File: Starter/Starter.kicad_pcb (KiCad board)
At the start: 2 copper layers, 114.3 x 88.9 mm, 51 parts, among them J1 AudioJack, J2 Speaker, J3 UART1, J4 Pot, J5 Conn_01x08_Pin, J6 GND, J7 DACOUT, SW1 UP, SW2 LEFT, SW3 DOWN, SW4 RGHT, U1 Adafruit ST7735R, U2 LP-MSPM0G3507, U3 MCP34119P, U4 HiLetGo_ST7735R, U5 ULN2003B, U6 TSOP31438

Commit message: update from sch
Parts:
- removed C1: 1uF, ECE319K:CP_Radial_Tantal200mil
- removed C2: 4.7uF, ECE319K:CP_Radial_Tantal200mil
- removed G***: LOGO, LOGO
- removed J1: AudioJack, ECE319K:Jack_3.5mm_CUI_SJ1-3523N_Horizontal
- removed J3: UART1, ECE319K:PinHeader_1x03_P2.54mm_Vertical
- removed J4: Pot, ECE319K:Testpoint_1x02_P2.54mm
- removed J6: GND, ECE319K:Testpoint_1x02_P2.54mm
- removed J7: DACOUT, ECE319K:Testpoint_1x02_P2.54mm
- removed JP1: TExaS, ECE319K:PinHeader_1x03_P2.54mm_Vertical
- removed R10: 12k, ECE319K:R_Axial_DIN0204_L3.6mm_D1.6mm_P7.62mm_Horizontal
- removed R17: 10k, ECE319K:R_Axial_DIN0204_L3.6mm_D1.6mm_P7.62mm_Horizontal
- removed U1: Adafruit ST7735R, ECE319K:adafruit_st7735r
- added C13: 0.1uF, Capacitor_SMD:C_0603_1608Metric_Pad1.08x0.95mm_HandSolder, F.Cu at (161.2, 124.7)
- added C14: 1uF, Capacitor_SMD:C_0603_1608Metric_Pad1.08x0.95mm_HandSolder, F.Cu at (161.2, 127.2)
- added C15: 4.7uF, Capacitor_SMD:C_0603_1608Metric_Pad1.08x0.95mm_HandSolder, F.Cu at (161.2, 129.7)
- added C16: 10nF, Capacitor_SMD:C_0603_1608Metric_Pad1.08x0.95mm_HandSolder, F.Cu at (165.5, 109.6)
- added C17: 0.1uF, Capacitor_SMD:C_0603_1608Metric_Pad1.08x0.95mm_HandSolder, F.Cu at (165.5, 112.1)
- added C18: 2.2uF, Capacitor_SMD:C_0603_1608Metric_Pad1.08x0.95mm_HandSolder, F.Cu at (165.5, 114.6)
- added C5: 0.1uF, Capacitor_SMD:C_0603_1608Metric_Pad1.08x0.95mm_HandSolder, F.Cu at (161.2, 114.6)
- added C6: 0.1uF, Capacitor_SMD:C_0603_1608Metric_Pad1.08x0.95mm_HandSolder, F.Cu at (161.2, 117.1)
- added C7: 0.1uF, Capacitor_SMD:C_0603_1608Metric_Pad1.08x0.95mm_HandSolder, F.Cu at (161.2, 119.7)
- added C8: 0.1uF, Capacitor_SMD:C_0603_1608Metric_Pad1.08x0.95mm_HandSolder, F.Cu at (161.2, 122.2)
- added D5: LED, LED_SMD:LED_0805_2012Metric, F.Cu at (189.4, 122.0)
- added D6: LED, LED_SMD:LED_0805_2012Metric, F.Cu at (189.4, 125.1)
- added D7: S1A, Diode_SMD:D_SMA, F.Cu at (189.2, 105.7)
- added M1: Vibration Motor, ECE319K:Testpoint_1x02_P2.54mm, F.Cu at (192.1, 98.6)
- added MT1: ICM-42670-P, ECE319K:XDCR_ICM-42670-P, F.Cu at (161.7, 144.4)
- added Q1: 2N2222, Package_TO_SOT_SMD:SOT-23, F.Cu at (189.6, 129.0)
- added R19: 1k, Resistor_SMD:R_0603_1608Metric_Pad0.98x0.95mm_HandSolder, F.Cu at (174.2, 112.1)
- added R20: 1k, Resistor_SMD:R_0603_1608Metric_Pad0.98x0.95mm_HandSolder, F.Cu at (174.2, 114.6)
- added R21: 1k, Resistor_SMD:R_0603_1608Metric_Pad0.98x0.95mm_HandSolder, F.Cu at (174.2, 117.1)
- added R22: 1k, Resistor_SMD:R_0603_1608Metric_Pad0.98x0.95mm_HandSolder, F.Cu at (174.2, 119.7)
- added R23: 10k, Resistor_SMD:R_0603_1608Metric_Pad0.98x0.95mm_HandSolder, F.Cu at (174.2, 122.2)
- added R24: 1k, Resistor_SMD:R_0603_1608Metric_Pad0.98x0.95mm_HandSolder, F.Cu at (174.2, 124.7)
- added R25: 10k, Resistor_SMD:R_0603_1608Metric_Pad0.98x0.95mm_HandSolder, F.Cu at (174.2, 127.2)
- added R26: 10k, Resistor_SMD:R_0603_1608Metric_Pad0.98x0.95mm_HandSolder, F.Cu at (174.2, 129.7)
- added TP2: 3V3, TestPoint:TestPoint_Pad_1.0x1.0mm, F.Cu at (189.5, 137.5)
- added TP3: UART1_TX, TestPoint:TestPoint_Pad_1.0x1.0mm, F.Cu at (189.5, 140.5)
- added TP4: UART2_RX, TestPoint:TestPoint_Pad_1.0x1.0mm, F.Cu at (189.5, 143.6)
- C3, C4: footprint ECE319K:C_Axial_200mil -> Capacitor_SMD:C_0603_1608Metric_Pad1.08x0.95mm_HandSolder
- D1, D2, D3, D4: footprint ECE319K:LED_D5.0mm -> LED_SMD:LED_0805_2012Metric
- H1, H2, H3, H4: value ~ -> MountingHole
- J2: footprint ECE319K:PinHeader_1x02_P2.54mm_Vertical -> ECE319K:Testpoint_1x02_P2.54mm
- R1, R11, R12, R13, R14, R15, R16, R18, R2, R3, R6: footprint ECE319K:R_Axial_DIN0204_L3.6mm_D1.6mm_P7.62mm_Horizontal -> Resistor_SMD:R_0603_1608Metric_Pad0.98x0.95mm_HandSolder
- R4: value 1.5k -> 750; footprint ECE319K:R_Axial_DIN0204_L3.6mm_D1.6mm_P7.62mm_Horizontal -> Resistor_SMD:R_0603_1608Metric_Pad0.98x0.95mm_HandSolder
- R5, R8: value 1.5k -> 470; footprint ECE319K:R_Axial_DIN0204_L3.6mm_D1.6mm_P7.62mm_Horizontal -> Resistor_SMD:R_0603_1608Metric_Pad0.98x0.95mm_HandSolder
- R7: value 1.5k -> 3k; footprint ECE319K:R_Axial_DIN0204_L3.6mm_D1.6mm_P7.62mm_Horizontal -> Resistor_SMD:R_0603_1608Metric_Pad0.98x0.95mm_HandSolder
- R9: value 12k -> 6k; footprint ECE319K:R_Axial_DIN0204_L3.6mm_D1.6mm_P7.62mm_Horizontal -> Resistor_SMD:R_0603_1608Metric_Pad0.98x0.95mm_HandSolder
- SW1, SW2, SW3: footprint ECE319K:SW_PUSH_6mm -> Button_Switch_SMD:SW_SPST_PTS645
- SW4: value RGHT -> RIGHT; footprint ECE319K:SW_PUSH_6mm -> Button_Switch_SMD:SW_SPST_PTS645
- TP1: value 3.3V -> GND; footprint ECE319K:Testpoint_1x02_P2.54mm -> TestPoint:TestPoint_Pad_1.0x1.0mm
- U2: moved to F.Cu
- U3: value MCP34119P -> MCP34119D
- U5: footprint ECE319K:DIP-16_W7.62mm -> ECE319K:SOIC127P600X175-16N
- moved U5 187.3 mm to (163.8, 136.7)
- moved D4 175.8 mm to (189.4, 119.0)
- moved U6 174.8 mm to (172.4, 133.4)
- moved R18 167.2 mm to (174.2, 109.6)
- moved U3 150.0 mm to (178.4, 135.0), turned to 0 degrees
- moved R16 146.4 mm to (169.9, 129.7)
- moved J2 144.2 mm to (187.4, 98.6)
- moved H1 142.9 mm to (179.5, 111.4)
- moved C4 142.8 mm to (161.2, 112.1)
- moved R14 142.5 mm to (169.9, 124.7), turned to 0 degrees
- moved R13 140.7 mm to (169.9, 122.2), turned to 0 degrees
- moved R12 140.7 mm to (169.9, 119.7), turned to 0 degrees
- moved R6 137.9 mm to (165.5, 129.7)
- moved R15 137.5 mm to (169.9, 127.2), turned to 0 degrees
- moved C3 129.7 mm to (161.2, 109.6), turned to 0 degrees
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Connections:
- net PA12 renamed /SDC_CS
- net PA13 renamed /TFT_DC
- net PB15 renamed /TFT_RST
- net PB6 renamed /TFT_CS
- net PB7 renamed /SPI_MISO
- net PB8 renamed /SPI_MOSI
- net PB9 renamed /SPI_SCK
- C3 pad 1: unconnected-(C3-Pad1) -> /DACOUT
- C3 pad 2: unconnected-(C3-Pad2) -> Net-(C3-Pad2)
- C4 pad 1: unconnected-(C4-Pad1) -> GND
- C4 pad 2: unconnected-(C4-Pad2) -> +3V3
- D1 pad 1: unconnected-(D1-K-Pad1) -> GND
- D1 pad 2: unconnected-(D1-A-Pad2) -> Net-(D1-A)
- D2 pad 1: unconnected-(D2-K-Pad1) -> GND
- D2 pad 2: unconnected-(D2-A-Pad2) -> Net-(D2-A)
- D3 pad 1: unconnected-(D3-K-Pad1) -> GND
- D3 pad 2: unconnected-(D3-A-Pad2) -> Net-(D3-A)
- D4 pad 1: unconnected-(D4-K-Pad1) -> Net-(D4-K)
- D4 pad 2: unconnected-(D4-A-Pad2) -> Net-(D4-A)
- H1 pad 1: unconnected-(H1-Hole-Pad1) -> (no net)
- H2 pad 1: unconnected-(H2-Hole-Pad1) -> (no net)
- H3 pad 1: unconnected-(H3-Hole-Pad1) -> (no net)
- H4 pad 1: unconnected-(H4-Hole-Pad1) -> (no net)
- J2 pad 1: unconnected-(J2-Pad1) -> Net-(U3-VO1)
- J2 pad 2: unconnected-(J2-Pad2) -> Net-(U3-VO2)
- J5 pad 1: unconnected-(J5-Pin_1-Pad1) -> /PB1
- J5 pad 2: unconnected-(J5-Pin_2-Pad2) -> /PB0
- J5 pad 3: unconnected-(J5-Pin_3-Pad3) -> /PA9/PB23
- J5 pad 4: unconnected-(J5-Pin_4-Pad4) -> /PB24
- J5 pad 5: unconnected-(J5-Pin_5-Pad5) -> /PA31
- J5 pad 6: unconnected-(J5-Pin_6-Pad6) -> /PA10
- J5 pad 7: unconnected-(J5-Pin_7-Pad7) -> /PA11
- J5 pad 8: unconnected-(J5-Pin_8-Pad8) -> /PB20
- R1 pad 1: unconnected-(R1-Pad1) -> /PB17
- R1 pad 2: unconnected-(R1-Pad2) -> Net-(D1-A)
- R11 pad 1: unconnected-(R11-Pad1) -> /DACOUT
- R11 pad 2: unconnected-(R11-Pad2) -> /DAC0
- R12 pad 1: unconnected-(R12-Pad1) -> Net-(R12-Pad1)
- R12 pad 2: unconnected-(R12-Pad2) -> GND
- R13 pad 1: unconnected-(R13-Pad1) -> Net-(R13-Pad1)
- R13 pad 2: unconnected-(R13-Pad2) -> GND
- R14 pad 1: unconnected-(R14-Pad1) -> Net-(R14-Pad1)
- R14 pad 2: unconnected-(R14-Pad2) -> GND
- R15 pad 1: unconnected-(R15-Pad1) -> Net-(R15-Pad1)
- R15 pad 2: unconnected-(R15-Pad2) -> GND
- R16 pad 1: unconnected-(R16-Pad1) -> Net-(U3-VIN)
- R16 pad 2: unconnected-(R16-Pad2) -> Net-(C3-Pad2)
- R18 pad 1: unconnected-(R18-Pad1) -> +5V
- R18 pad 2: unconnected-(R18-Pad2) -> Net-(D4-A)
- R2 pad 1: unconnected-(R2-Pad1) -> /PB16
- R2 pad 2: unconnected-(R2-Pad2) -> Net-(D2-A)
- R3 pad 1: unconnected-(R3-Pad1) -> /PB13
- R3 pad 2: unconnected-(R3-Pad2) -> Net-(D3-A)
- R4 pad 1: unconnected-(R4-Pad1) -> /DACOUT
- R4 pad 2: unconnected-(R4-Pad2) -> /DAC4
- R5 pad 1: unconnected-(R5-Pad1) -> /PB19
- R5 pad 2: unconnected-(R5-Pad2) -> Net-(D5-A)
- R6 pad 1: unconnected-(R6-Pad1) -> /DACOUT
- R6 pad 2: unconnected-(R6-Pad2) -> /DAC3
- R7 pad 1: unconnected-(R7-Pad1) -> /DACOUT
- R7 pad 2: unconnected-(R7-Pad2) -> /DAC2
- R8 pad 1: unconnected-(R8-Pad1) -> /PB12
- R8 pad 2: unconnected-(R8-Pad2) -> Net-(D6-A)
- R9 pad 1: unconnected-(R9-Pad1) -> /DACOUT
- R9 pad 2: unconnected-(R9-Pad2) -> /DAC1
- RV1 pad 1: unconnected-(RV1-Pad1) -> GND
- RV1 pad 2: unconnected-(RV1-Pad2) -> /PB18
- RV1 pad 3: unconnected-(RV1-Pad3) -> +3V3
- SW1 pad 1: unconnected-(SW1-Pad1) -> Net-(R12-Pad1)
- SW1 pad 2: unconnected-(SW1-Pad2) -> +3V3
- SW2 pad 1: unconnected-(SW2-Pad1) -> Net-(R13-Pad1)
- SW2 pad 2: unconnected-(SW2-Pad2) -> +3V3
- SW3 pad 1: unconnected-(SW3-Pad1) -> Net-(R14-Pad1)
- SW3 pad 2: unconnected-(SW3-Pad2) -> +3V3
- SW4 pad 1: unconnected-(SW4-Pad1) -> Net-(R15-Pad1)
- SW4 pad 2: unconnected-(SW4-Pad2) -> +3V3
- TP1 pad 1: +3V3 -> GND
- U2 pad J1_10: PB3 -> /I2C_SDA
- U2 pad J1_2: PA25 -> /DAC3
- U2 pad J1_3: PB23 -> /PA9/PB23
- U2 pad J1_4: PA8 -> /UART1_TX
- U2 pad J1_5: PA26 -> /DAC2
- U2 pad J1_6: PB24 -> /PB24
- U2 pad J1_8: PA27 -> /DAC1
- U2 pad J1_9: PB2 -> /I2C_SCL
- U2 pad J2_10: PB16 -> /PB16
- U2 pad J2_2: PB12 -> /PB12
- U2 pad J2_3: PB17 -> /PB17
- U2 pad J2_9: PB0 -> /PB0
- U2 pad J3_10: PA15 -> /PA15
- U2 pad J3_3: PB19 -> /PB19
- U2 pad J3_4: PA22 -> /UART2_RX
- U2 pad J3_5: PB18 -> /PB18
- U2 pad J3_6: PA18 -> /PA18
- U2 pad J3_7: PA24 -> /DAC4
- U2 pad J3_8: PA17 -> /PA17
- U2 pad J3_9: PA16 -> /PA16
- U2 pad J4_1: PB4 -> /MTR_PWM
- U2 pad J4_2: PB1 -> /PB1
- U2 pad J4_3: PA28 -> /DAC0
- U2 pad J4_4: PA31 -> /PA31
- U2 pad J4_5: PB20 -> /PB20
- U2 pad J4_6: PB13 -> /PB13
- U2 pad J4_7: PA10 -> /PA10
- U2 pad J4_8: PA11 -> /PA11
- U3 pad 1: unconnected-(U3-CD-Pad1) -> GND
- U3 pad 2: unconnected-(U3-FC2-Pad2) -> Net-(U3-FC2)
- U3 pad 3: unconnected-(U3-FC1-Pad3) -> Net-(U3-FC1)
- U3 pad 4: unconnected-(U3-VIN-Pad4) -> Net-(U3-VIN)
- U3 pad 5: unconnected-(U3-VO1-Pad5) -> Net-(U3-VO1)
- U3 pad 6: unconnected-(U3-Vcc-Pad6) -> +5V
- U3 pad 7: unconnected-(U3-GND-Pad7) -> GND
- U3 pad 8: unconnected-(U3-VO2-Pad8) -> Net-(U3-VO2)
- U5 pad 1: unconnected-(U5-1B-Pad1) -> /UART1_TX
- U5 pad 16: unconnected-(U5-1C-Pad16) -> Net-(D4-K)
- U5 pad 8: unconnected-(U5-E-Pad8) -> GND
- U6 pad 1: unconnected-(U6-Gnd-Pad1) -> GND
- U6 pad 2: unconnected-(U6-Vs-Pad2) -> +3V3
- U6 pad 3: unconnected-(U6-Out-Pad3) -> /UART2_RX
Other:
- board outline removed
- board text removed: "DACOUT"
- board text removed: "ECE319K PCB camp Spring 2025"
- board text removed: "GND"
- board text removed: "POT"
- board text removed: "TExaS"
- board text removed: "U1Rx"
- board text removed: "U1Tx"
- board text removed: "Your names"

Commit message: initial layout
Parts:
- removed TP1: GND, TestPoint:TestPoint_Pad_1.0x1.0mm
- removed TP2: 3V3, TestPoint:TestPoint_Pad_1.0x1.0mm
- removed TP3: UART1_TX, TestPoint:TestPoint_Pad_1.0x1.0mm
- removed TP4: UART2_RX, TestPoint:TestPoint_Pad_1.0x1.0mm
- C13, C16, C17, C18, D7, M1, MT1, Q1, R24, R25, R26, U2, U5: moved to B.Cu
- D4: footprint LED_SMD:LED_0805_2012Metric -> ECE319K:LED_D5.0mm
- H1, H2, H3, H4: footprint ECE319K:MountingHole_4_40 -> MountingHole:MountingHole_3.2mm_M3
- moved H1 158.7 mm to (22.8, 86.1)
- moved H2 158.7 mm to (22.8, 92.2)
- moved H3 158.7 mm to (22.8, 98.4)
- moved H4 158.7 mm to (22.8, 104.5)
- moved J2 112.4 mm to (76.5, 80.2)
- moved C14 108.2 mm to (242.0, 55.2)
- moved C15 108.2 mm to (242.0, 57.8)
- moved C3 108.2 mm to (242.0, 37.7)
- moved C4 108.2 mm to (242.0, 40.2)
- moved C5 108.2 mm to (242.0, 42.7)
- moved C6 108.2 mm to (242.0, 45.2)
- moved C7 108.2 mm to (242.0, 47.7)
- moved C8 108.2 mm to (242.0, 50.2)
- moved R1 108.2 mm to (246.4, 45.2)
- moved R11 108.2 mm to (250.7, 45.2)
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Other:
- board outline added: 139.7 x 72.5 mm

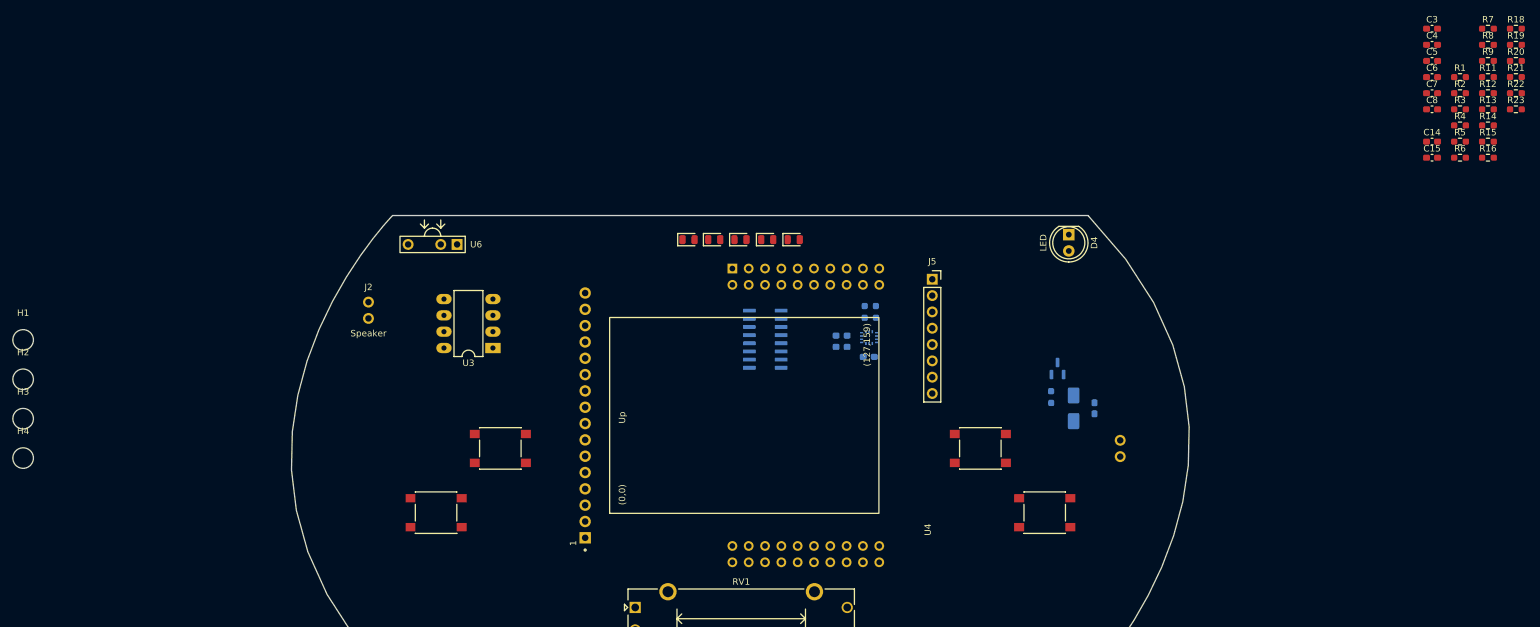
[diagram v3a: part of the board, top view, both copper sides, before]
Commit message: Component placements finalized
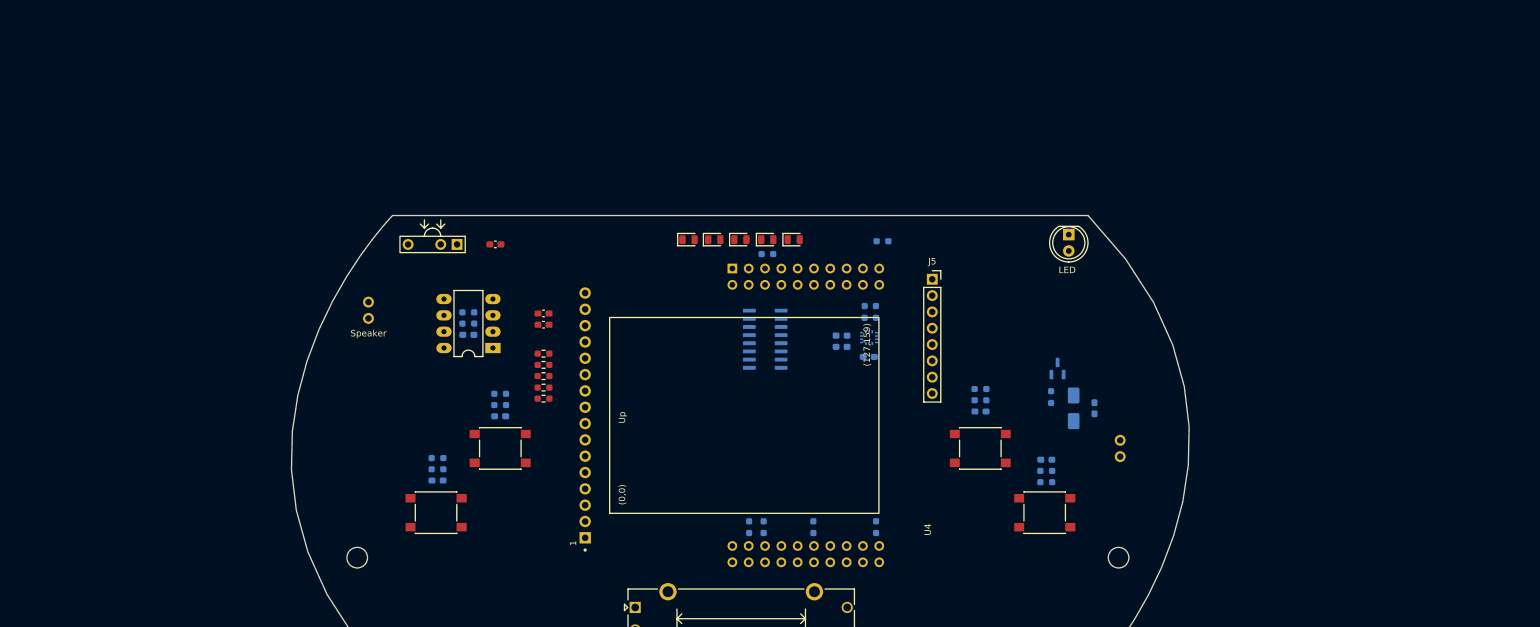
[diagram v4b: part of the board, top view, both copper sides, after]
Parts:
- removed H3, H4: MountingHole, MountingHole:MountingHole_3.2mm_M3
- C3, C5, C6, C7, C8, R1, R12, R13, R14, R15, R16, R18, R19, R2, R20, R21, R22, R23, R3, R5, R8: moved to B.Cu
- moved R20 179.5 mm to (87.2, 106.2), turned to 180 degrees
- moved H2 172.7 mm to (193.2, 120.0)
- moved R13 172.3 mm to (87.2, 104.5), turned to 180 degrees
- moved R19 167.7 mm to (97.0, 96.2), turned to 180 degrees
- moved C6 167.0 mm to (87.2, 108.0), turned to 180 degrees
- moved R23 166.1 mm to (92.0, 81.8)
- moved R16 160.8 mm to (92.0, 83.6), turned to 180 degrees
- moved R12 160.7 mm to (97.0, 94.5), turned to 180 degrees
- moved C3 157.4 mm to (92.0, 85.3), turned to 180 degrees
- moved R7 155.4 mm to (103.8, 88.2)
- moved C5 155.2 mm to (97.0, 98.0), turned to 180 degrees
- moved R9 154.4 mm to (103.8, 90.0)
- moved R11 154.2 mm to (103.8, 91.8)
- moved C4 149.1 mm to (96.2, 71.2)
- moved R4 148.4 mm to (103.8, 93.5)
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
